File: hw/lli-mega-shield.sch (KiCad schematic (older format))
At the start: 28 parts, among them J1 DB25, P1 Enable, Q1 NPN, U1 APC220, U2 LM35, U5 ADIS16405, U6 R-78B5.0-1.5, U7 UP500/UP501

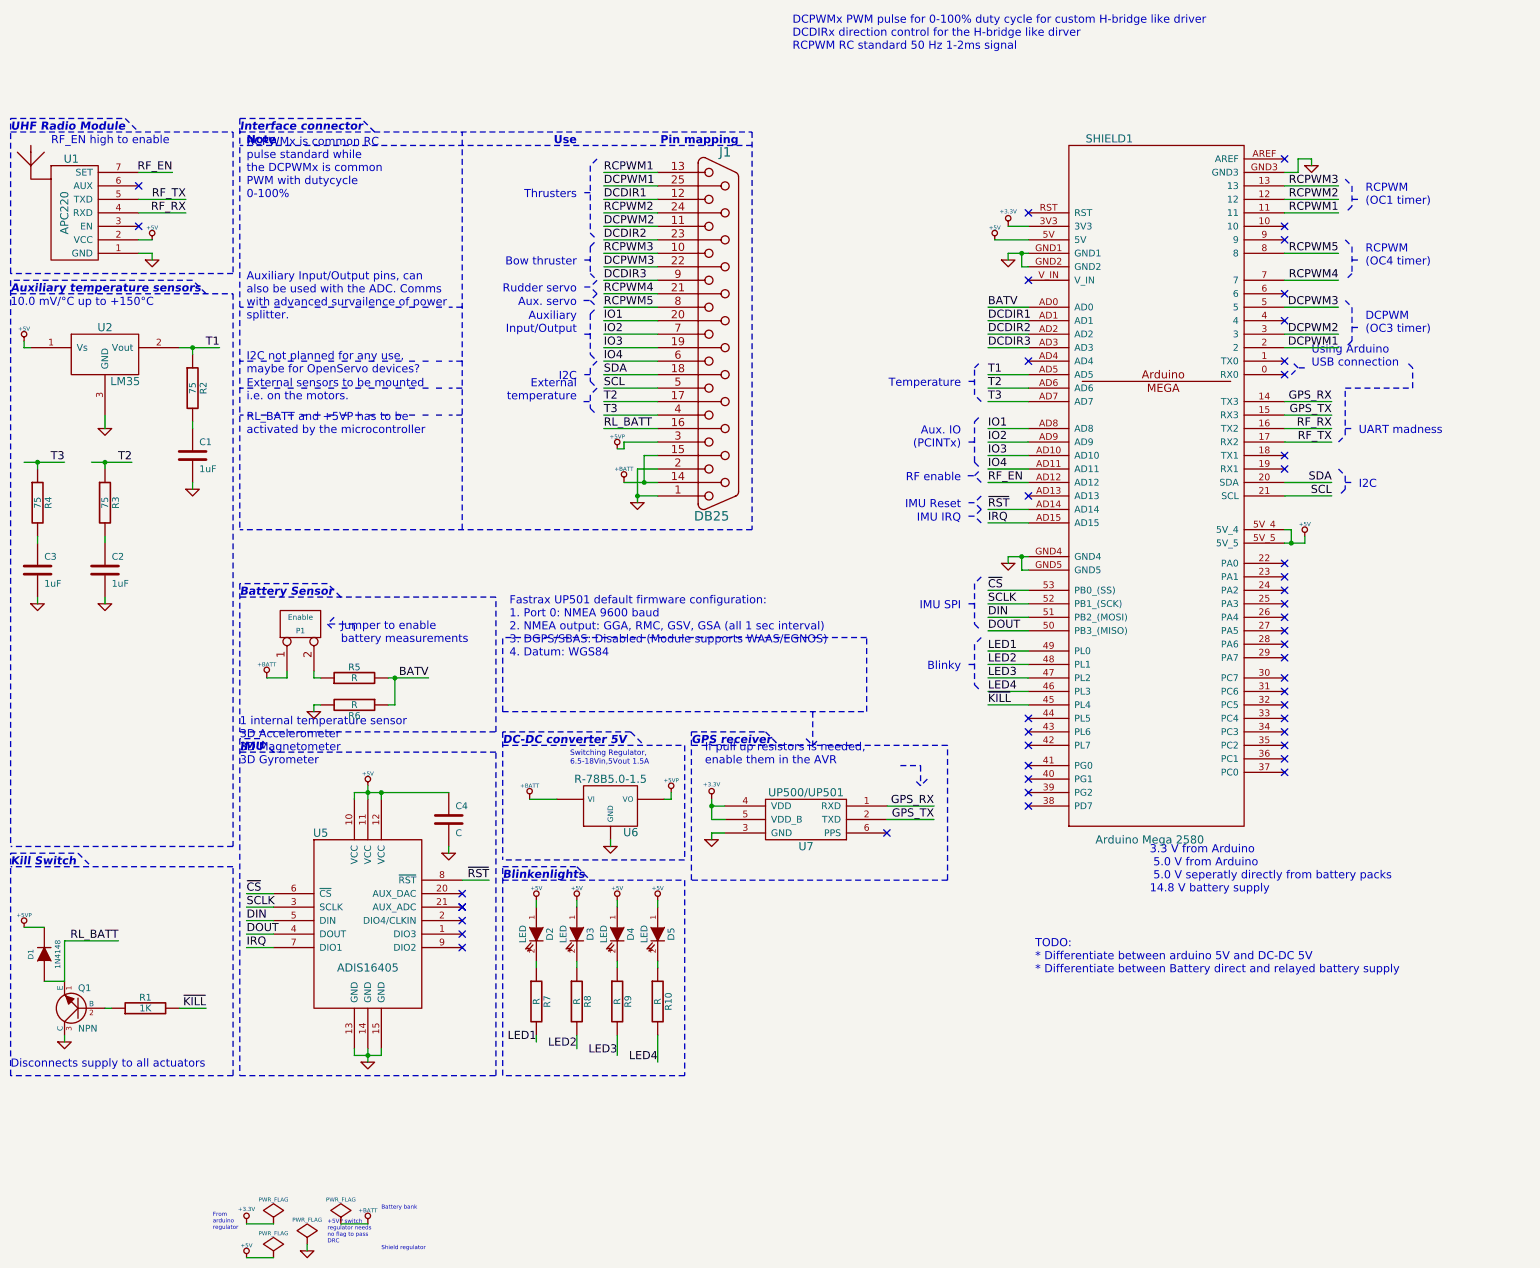
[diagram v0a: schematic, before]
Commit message: Changed regulator footprint
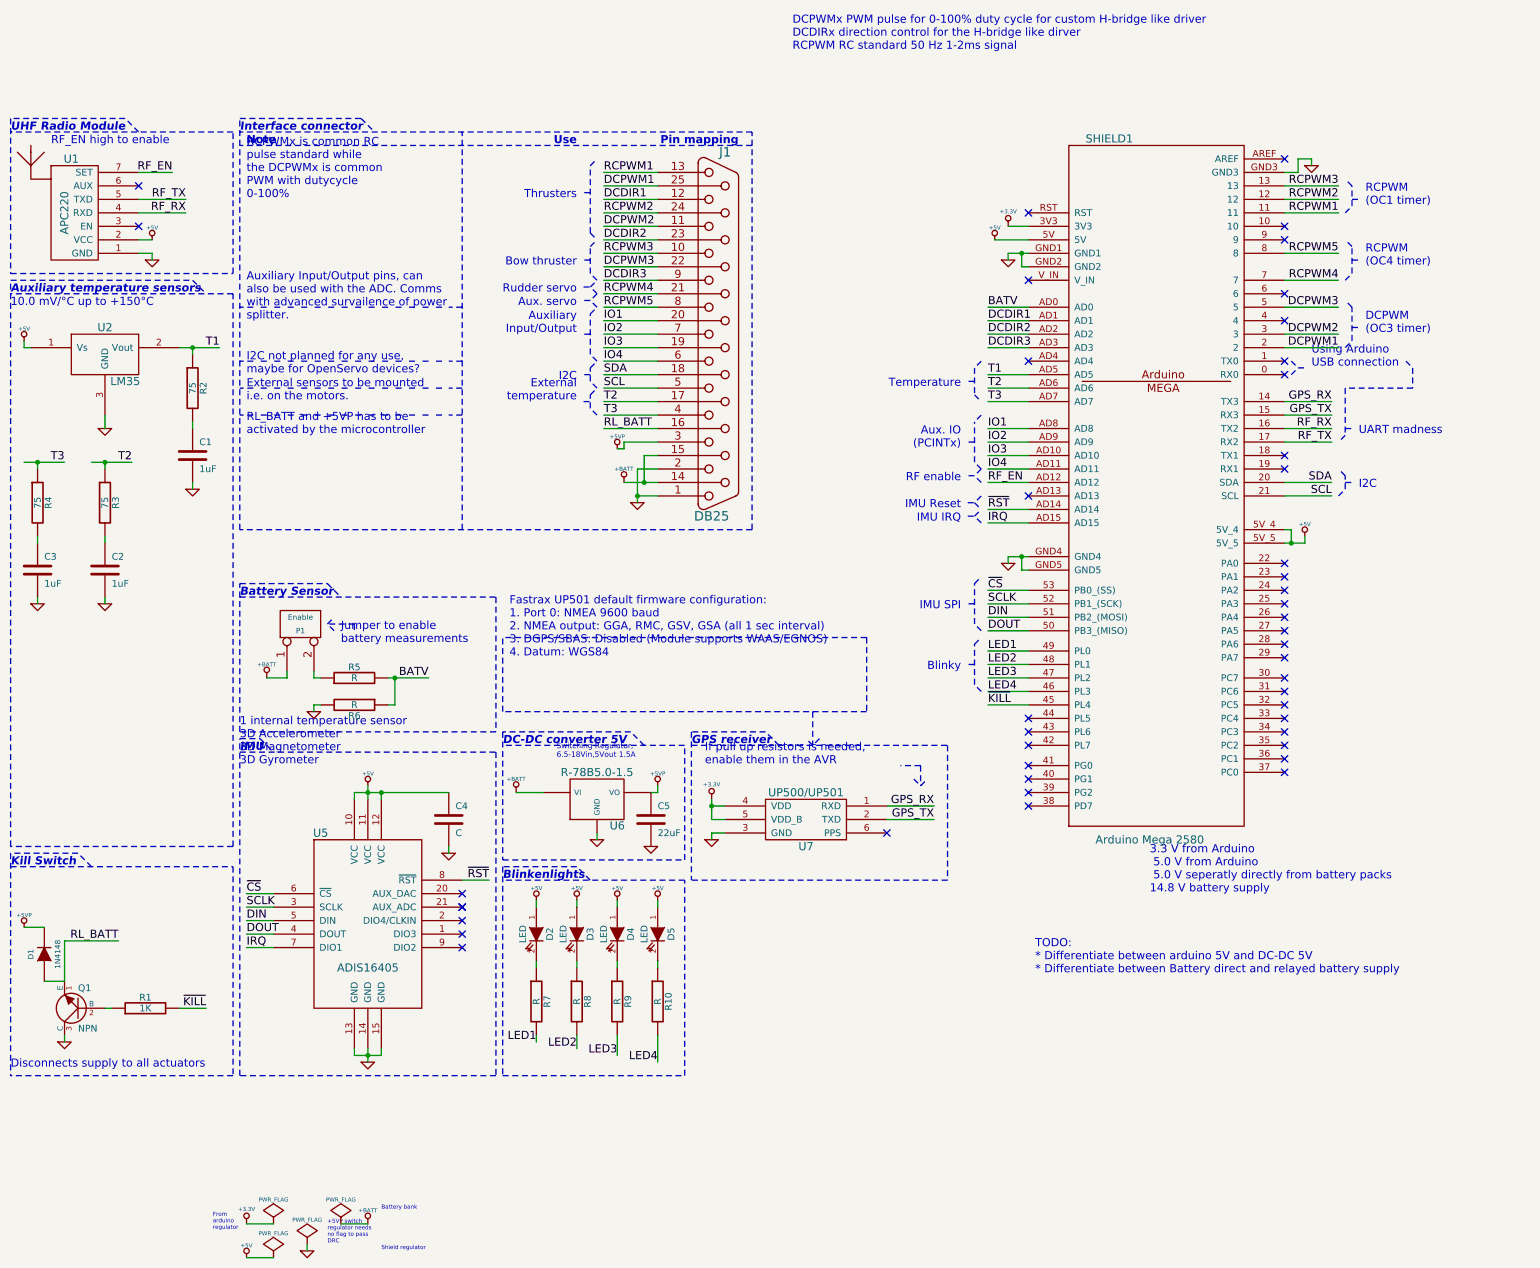
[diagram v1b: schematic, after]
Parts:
- added C5: 22uF, symbol C
- U6: value R-78B5.0-1.5 -> R-78B5.0-1.5
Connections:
- net +5VP: now also C5.1
- net GND: now also C5.2
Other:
- moved on the sheet: U6

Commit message: PCB almost finished
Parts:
- C4: value C -> C42
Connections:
- net +5VP: now also J1.16 (P16); no longer J1.3
- net DCDIR1: now also J1.4, SHIELD1.AD2; no longer J1.12, SHIELD1.AD1
- net DCDIR2: now also J1.5, SHIELD1.AD3; no longer J1.23 (P23), SHIELD1.AD2
- net DCDIR3: now also J1.6, SHIELD1.AD4; no longer J1.9, SHIELD1.AD3
- net DCPWM1: now also J1.24 (P24); no longer J1.25 (P25)
- net DCPWM2: now also J1.23 (P23); no longer J1.11
- net IO1: now also J1.9; no longer J1.20 (P20)
- net IO2: now also J1.10; no longer J1.7
- net IO3: now also J1.11; no longer J1.19 (P19)
- net IO4: now also J1.12; no longer J1.6
- net RCPWM1: now also J1.19 (P19); no longer J1.13
- net RCPWM2: now also J1.18 (P18); no longer J1.24 (P24)
- net RCPWM3: now also J1.17 (P17); no longer J1.10
- net RCPWM5: now also J1.20 (P20); no longer J1.8
- net RL_BATT: now also J1.3; no longer J1.16 (P16)
- net SCL: now also J1.13; no longer J1.5
- net SDA: now also J1.25 (P25); no longer J1.18 (P18)
- net T2: now also J1.7; no longer J1.17 (P17)
- net T3: now also J1.8; no longer J1.4
- net ~KILL: now also SHIELD1.AD1; no longer SHIELD1.45 (PL4)

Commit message: Some minor mods and notes on hw
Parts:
- C4: value C42 -> 100nF
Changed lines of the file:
@@
-EESchema Schematic File Version 2  date tir 09 okt 2012 11:29:43 CEST
+EESchema Schematic File Version 2  date fre 16 nov 2012 21:09:53 CET
 LIBS:power
 LIBS:device
@@
 Sheet 1 1
 Title "Low Level Interface"
-Date "9 oct 2012"
+Date "16 nov 2012"
 Rev "1"
 Comp "Aalborg University"
@@
 P 3800 5800
 F 0 "C4" H 3850 5900 50  0000 L CNN
-F 1 "C42" H 3850 5700 50  0000 L CNN
+F 1 "100nF" H 3850 5700 50  0000 L CNN
 	1    3800 5800
 	1    0    0    -1

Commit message: Subtle changes to LLI hw
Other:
- note removed: "TODO:\n* Differentiate between arduino 5V and DC-DC 5V\n* Differentiate between Battery direct and relayed battery supply"
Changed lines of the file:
@@
-EESchema Schematic File Version 2  date fre 16 nov 2012 21:09:53 CET
+EESchema Schematic File Version 2  date ons 28 nov 2012 13:28:42 CET
 LIBS:power
 LIBS:device
@@
 Sheet 1 1
 Title "Low Level Interface"
-Date "16 nov 2012"
+Date "28 nov 2012"
 Rev "1"
 Comp "Aalborg University"
@@
 Text Label 5350 7600 2    60   ~ 0
 LED4
-Text Notes 8150 6950 0    60   ~ 0
-TODO:\n* Differentiate between arduino 5V and DC-DC 5V\n* Differentiate between Battery direct and relayed battery supply
 Text Notes 2300 2100 0    60   ~ 0
 Auxiliary Input/Output pins, can\nalso be used with the ADC. Comms\nwith advanced survailence of power\nsplitter.

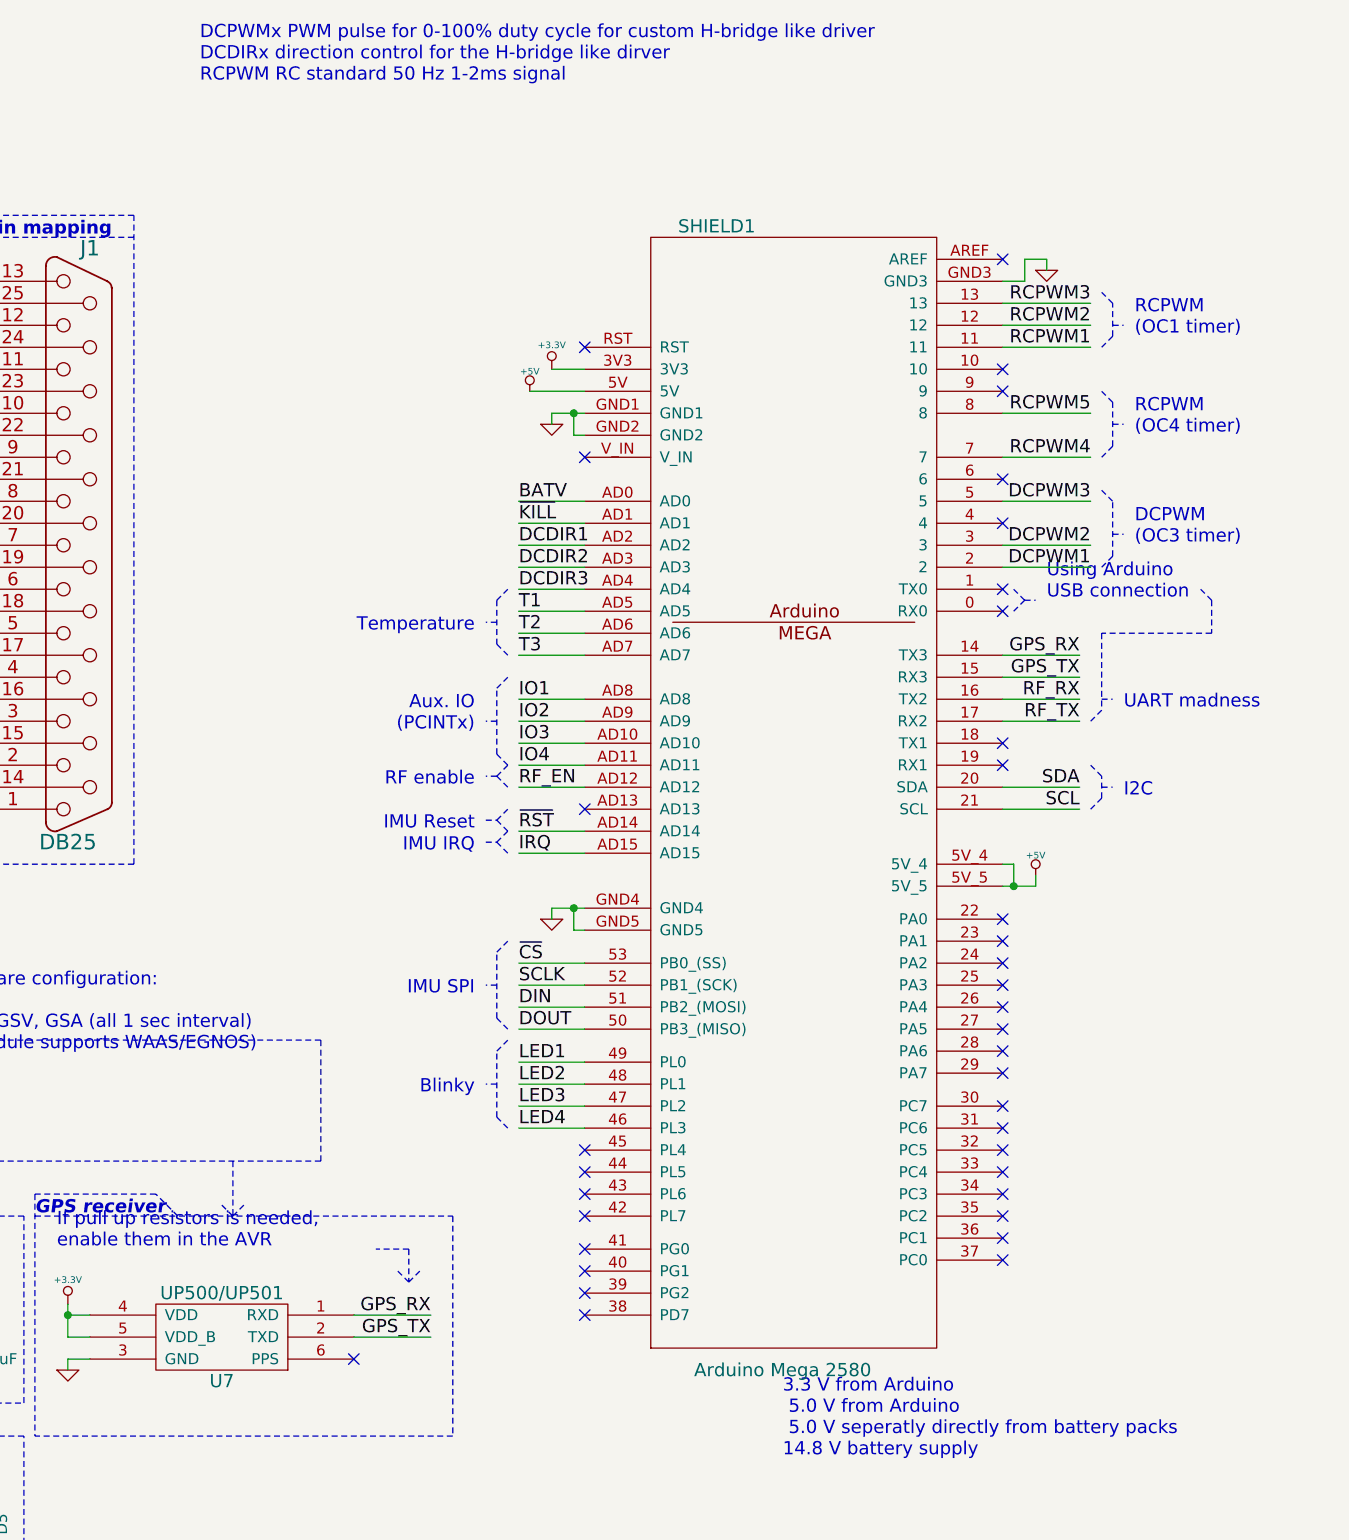
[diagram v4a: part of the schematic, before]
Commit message: Added Openlogger to LLI board
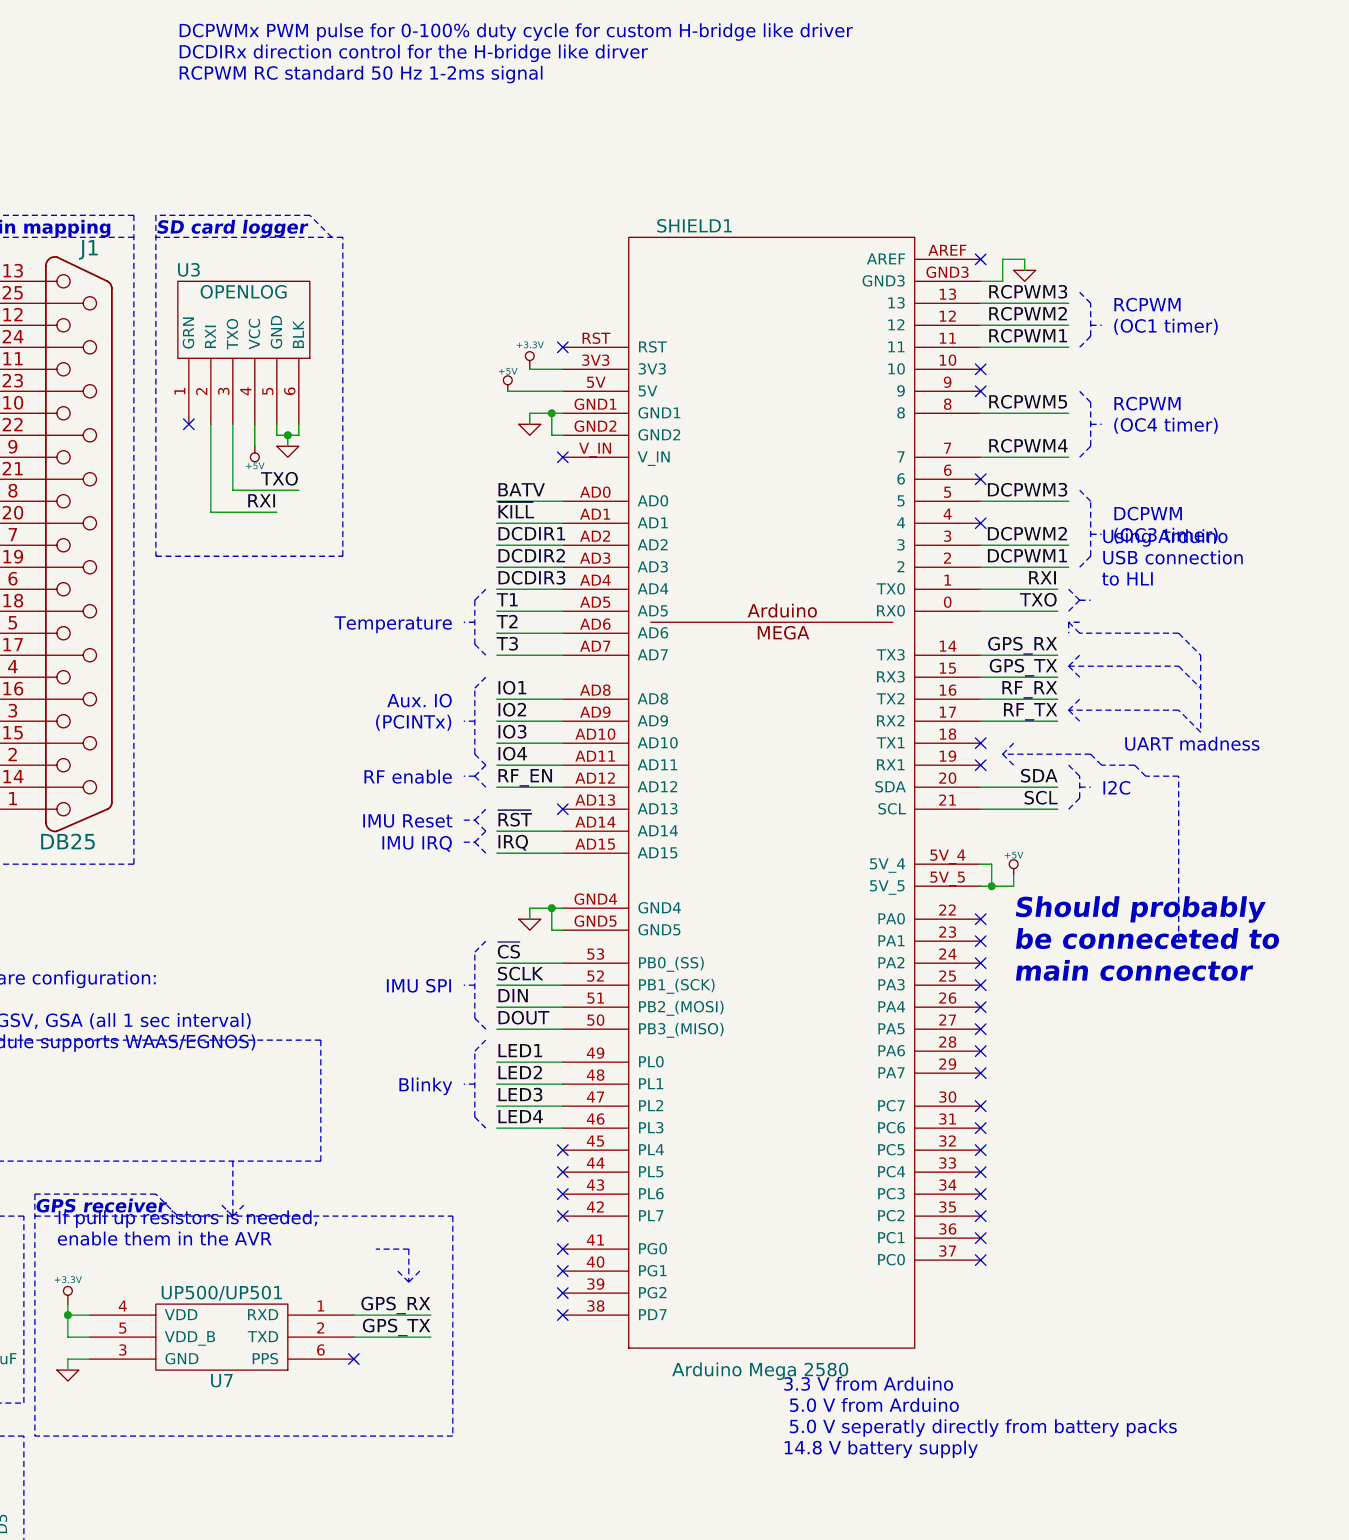
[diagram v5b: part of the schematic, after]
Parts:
- added U3: OPENLOG, symbol OPENLOG
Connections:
- net +5V: now also U3.4 (VCC)
- net GND: now also U3.5 (GND), U3.6 (BLK)
- net TXO: now reaches SHIELD1.0 (RX0)
- net TXO: now also U3.3 (TXO)
- net RXI: now reaches SHIELD1.1 (TX0)
- net RXI: now also U3.2 (RXI)
- no-connect marks 45 -> 44
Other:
- note added: "SD card logger"
- note added: "Should probably\nbe conneceted to\nmain connector"
- note added: "Using Arduino\nUSB connection\nto HLI"
- note removed: "Using Arduino\nUSB connection"
- moved on the sheet: SHIELD1
